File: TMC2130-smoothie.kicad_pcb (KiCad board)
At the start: 4 copper layers, 55 parts, among them P1 CONN_01X04, U1 TMC2130

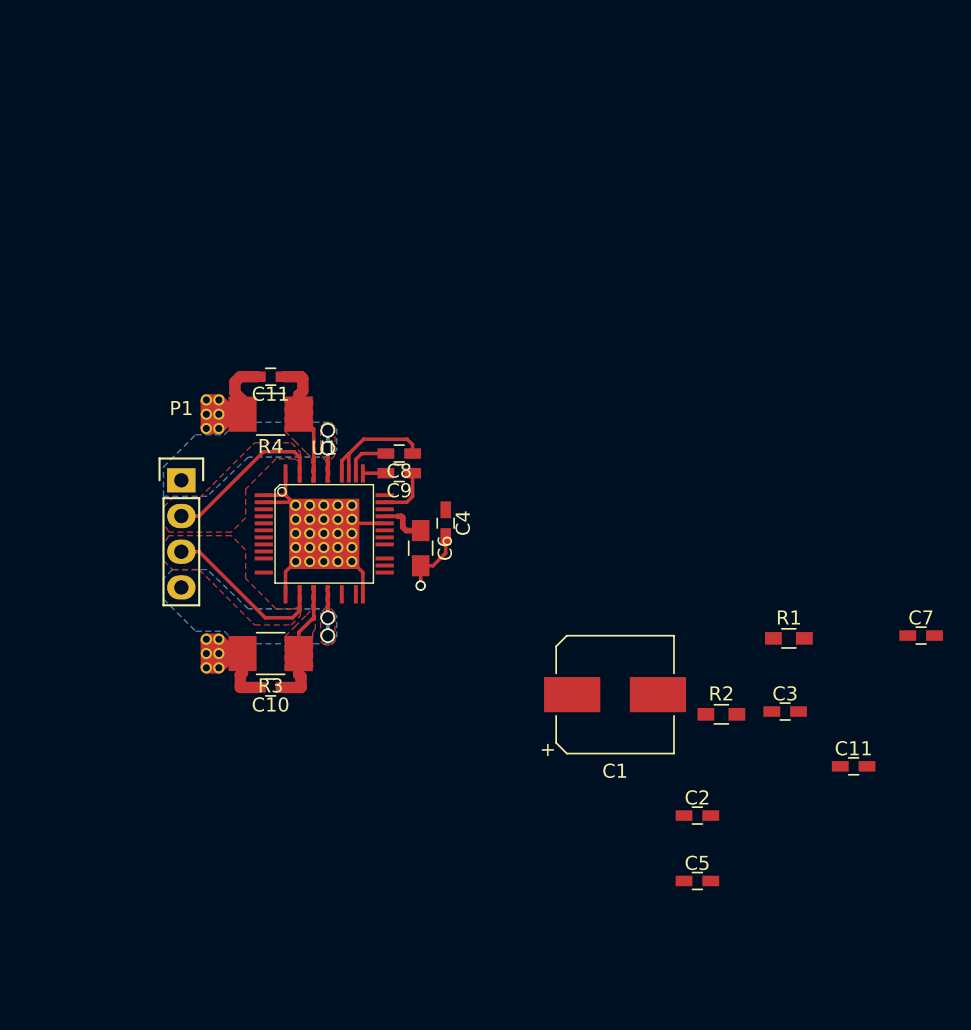
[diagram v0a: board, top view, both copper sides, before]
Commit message: Initial layout of 1-driver
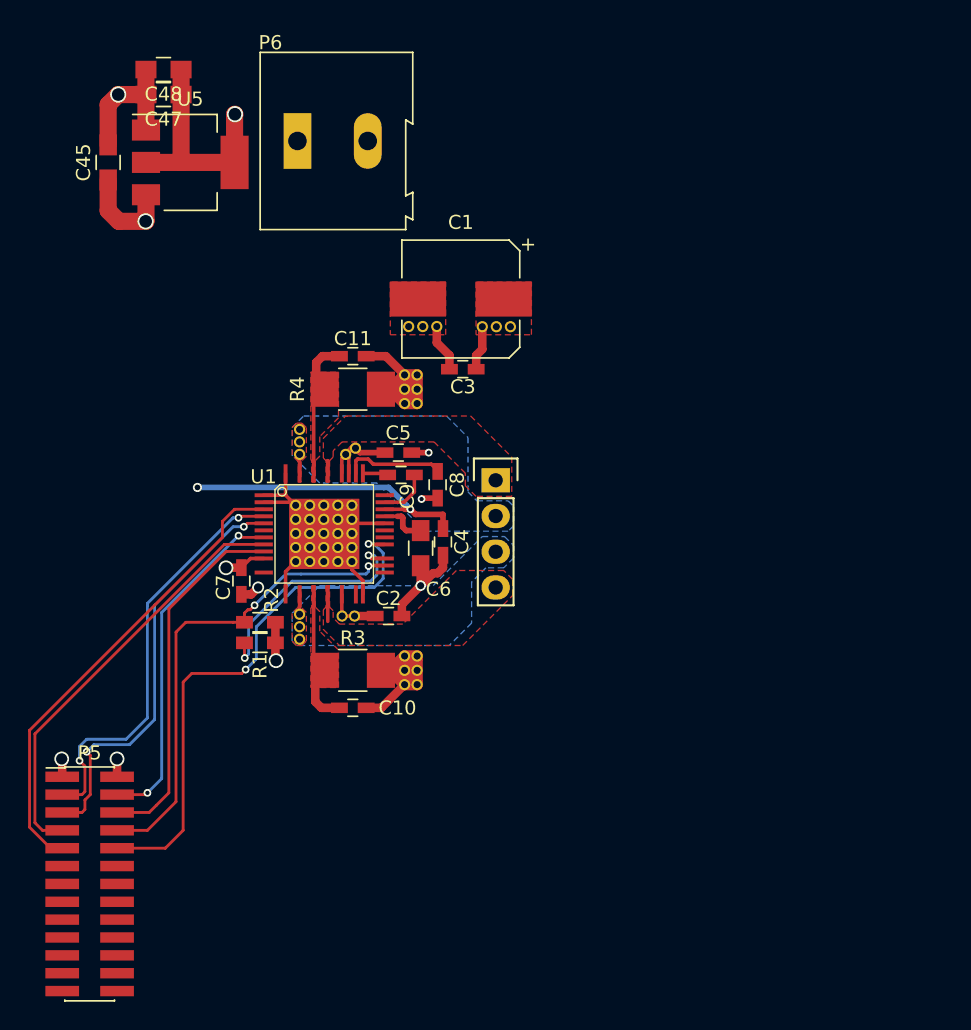
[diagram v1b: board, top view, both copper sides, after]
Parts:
- removed the C10 at (250.2, 163.3)
- added C45: 10uF, Capacitors_SMD:C_0805_HandSoldering, F.Cu at (238.6, 126.0)
- added C47: 10uF, Capacitors_SMD:C_0805_HandSoldering, F.Cu at (242.6, 121.2)
- added C48: 10uF, Capacitors_SMD:C_0805_HandSoldering, F.Cu at (242.6, 119.4)
- added P5: CONN_01X26, Pin_Headers:Pin_Header_Straight_2x13_Pitch1.27mm_SMD, F.Cu at (237.3, 177.3)
- added P6: Vmot, Connect:AK300-2, F.Cu at (252.1, 124.5)
- added REF**: VIA 0.5d0.8p, VIA 0.5d0.8p, F.Cu at (256.2, 146.3)
- added REF**: VIA 0.5d0.8p, VIA 0.5d0.8p, F.Cu at (252.2, 145.9)
- added REF**: VIA 0.5d0.8p, VIA 0.5d0.8p, F.Cu at (252.2, 145.0)
- added REF**: VIA 0.5d0.8p, VIA 0.5d0.8p, F.Cu at (252.2, 146.7)
- added REF**: VIA 0.5d0.8p, VIA 0.5d0.8p, F.Cu at (255.5, 146.7)
- added REF**: VIA 0.5d0.8p, VIA 0.5d0.8p, F.Cu at (256.2, 158.2)
- added REF**: VIA 0.5d0.8p, VIA 0.5d0.8p, F.Cu at (255.3, 158.2)
- added REF**: VIA 0.5d0.8p, VIA 0.5d0.8p, F.Cu at (252.2, 159.0)
- added REF**: VIA 0.5d0.8p, VIA 0.5d0.8p, F.Cu at (252.2, 158.1)
- added REF**: VIA 0.5d0.8p, VIA 0.5d0.8p, F.Cu at (252.2, 159.9)
- added REF**11111: VIA 0.5d0.8p, VIA 0.5d0.8p, F.Cu at (265.2, 137.7)
- added REF**11121: VIA 0.5d0.8p, VIA 0.5d0.8p, F.Cu at (266.2, 137.7)
- added REF**11131: VIA 0.5d0.8p, VIA 0.5d0.8p, F.Cu at (267.2, 137.7)
- added REF**121: VIA 0.5d0.8p, VIA 0.5d0.8p, F.Cu at (260.0, 137.7)
- added REF**131: VIA 0.5d0.8p, VIA 0.5d0.8p, F.Cu at (261.0, 137.7)
- added REF**141: VIA 0.5d0.8p, VIA 0.5d0.8p, F.Cu at (262.0, 137.7)
- added U5: AP1117-3v3, TO_SOT_Packages_SMD:SOT-223-3Lead_TabPin2, F.Cu at (244.5, 126.0)
- moved C7 48.5 mm to (248.1, 155.8), turned to 270 degrees
- moved C11 46.0 mm to (256.0, 139.8)
- moved R2 37.6 mm to (249.4, 158.7)
- moved C5 37.1 mm to (259.3, 146.6)
- moved C3 33.4 mm to (263.9, 140.7), turned to 180 degrees
- moved R1 33.2 mm to (249.4, 160.1)
- moved C1 30.2 mm to (263.7, 135.7), turned to 180 degrees
- moved C2 26.1 mm to (258.6, 158.2)
- moved REF** 25.7 mm to (260.6, 141.1), turned to 180 degrees
- moved REF** 25.2 mm to (260.6, 163.1), turned to 180 degrees
- moved REF** 24.7 mm to (259.7, 141.1), turned to 180 degrees
- moved C10 24.3 mm to (256.0, 164.8), turned to 0 degrees
- moved REF** 24.2 mm to (259.7, 163.1), turned to 180 degrees
- moved REF** 24.0 mm to (260.6, 142.1), turned to 180 degrees
- moved REF** 23.6 mm to (260.6, 162.1), turned to 180 degrees
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- renumbered C11 to C10, R2 to R1, R1 to R2, R4 to R3, R3 to R4
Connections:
- C10 pad 1: Net-(C11-Pad1) -> Net-(C10-Pad1)
- C7 pad 1: Net-(C7-Pad1) -> +3V3
- R1 pad 1: M1_DIAG0 -> M1_DIAG1
- R2 pad 1: M1_DIAG1 -> M1_DIAG0
- R3 pad 1: Net-(C11-Pad1) -> Net-(C10-Pad1)
- R4 pad 1: Net-(C10-Pad1) -> Net-(C11-Pad1)
- U1 pad 10: Net-(C7-Pad1) -> +3V3
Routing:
- net M1_EN: track 0.00 -> 38.7 mm, vias 0 -> 2
- net M1_DIAG0: track 0.00 -> 34.5 mm, vias 0 -> 2
- net SPI_CS_M1: track 0.00 -> 33.7 mm
- net M1_STEP: track 0.00 -> 30.3 mm
- net SPI_MOSI: track 0.00 -> 30.2 mm, vias 0 -> 2
- net SPI_SCK: track 0.00 -> 29.7 mm, vias 0 -> 2
- net +5V: track 0.00 -> 29.4 mm, vias 0 -> 4
- net M1_DIR: track 0.00 -> 25.8 mm
- net SPI_MISO: track 0.00 -> 25.0 mm, vias 0 -> 2
- net +3V3: track 0.00 -> 22.1 mm, vias 0 -> 3
- net M1_DIAG1: track 0.00 -> 17.3 mm, vias 0 -> 2
- net GND: track 66.1 -> 82.0 mm, vias 1 -> 5
- net /Driver1/OB1: track 11.7 -> 1.42 mm
- net /Driver1/OA1: track 11.6 -> 1.35 mm
- net +24V: track 8.76 -> 14.3 mm, vias 0 -> 1
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- added copper zone on F.Cu, net +24V
- added copper zone on In2.Cu, net +24V
- added copper zone on In2.Cu, net +3V3
- added copper zone on In2.Cu, net +5V
- added copper zone on B.Cu, net /Driver1/OA1
- added copper zone on B.Cu, net /Driver1/OB1
- added copper zone on F.Cu, net GND
- removed copper zone on B.Cu, net /Driver1/OA2
- removed copper zone on B.Cu, net /Driver1/OB2

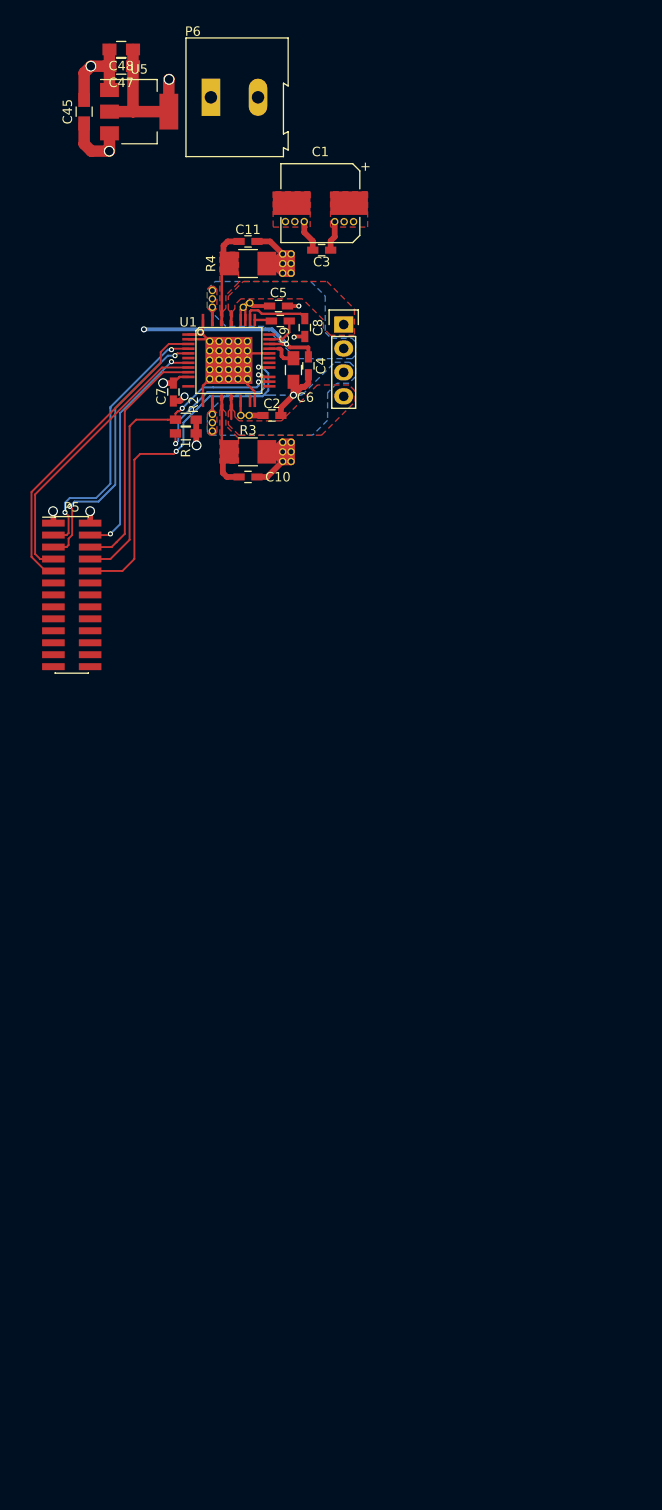
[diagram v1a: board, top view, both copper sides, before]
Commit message: Routed entire PCB
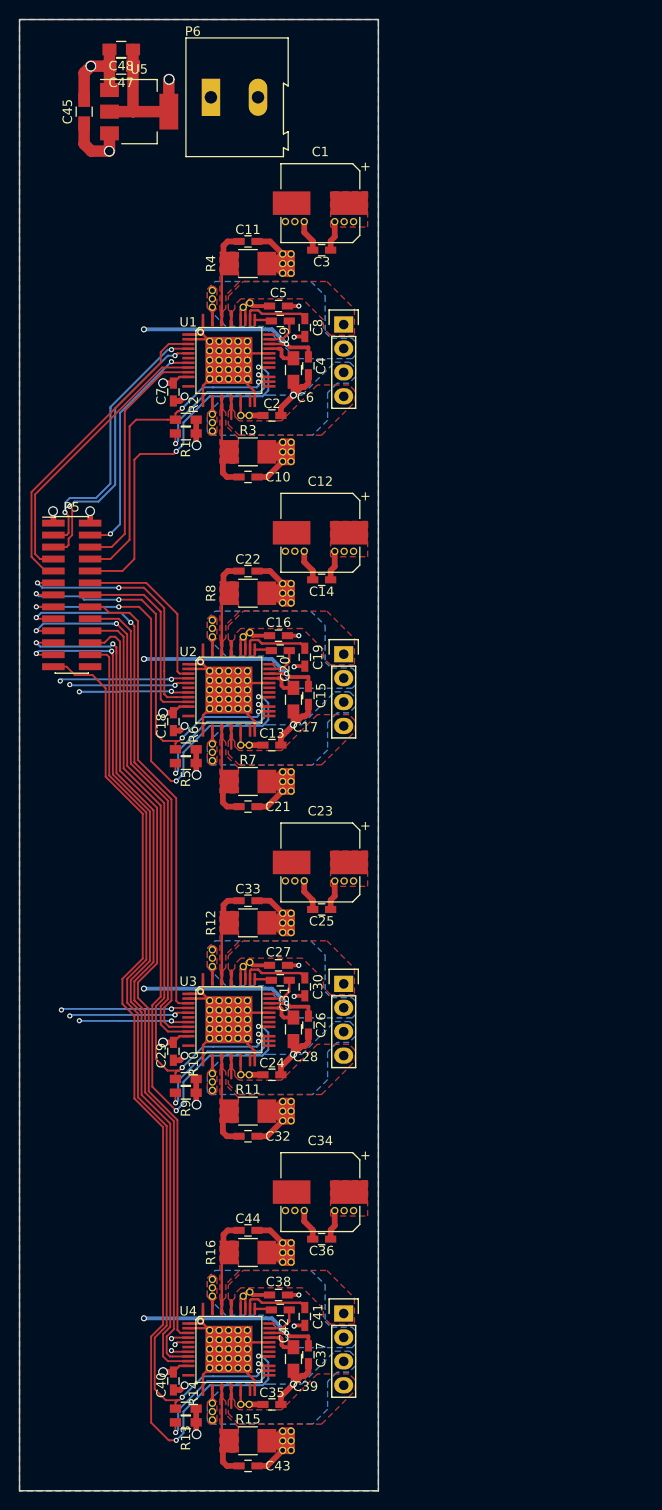
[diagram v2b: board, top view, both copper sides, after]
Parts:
- added C12: 100uF, Capacitors_SMD:CP_Elec_8x10, F.Cu at (263.7, 170.7)
- added C13: 100nF, Capacitors_SMD:C_0603_HandSoldering, F.Cu at (258.6, 193.2)
- added C14: 100nF, Capacitors_SMD:C_0603_HandSoldering, F.Cu at (263.9, 175.7)
- added C15: 470nF, Capacitors_SMD:C_0603_HandSoldering, F.Cu at (262.4, 188.0)
- added C16: 100nF, Capacitors_SMD:C_0603_HandSoldering, F.Cu at (259.3, 181.6)
- added C17: 4.7uF, Capacitors_SMD:C_0805_HandSoldering, F.Cu at (260.9, 188.4)
- added C18: 100nF, Capacitors_SMD:C_0603_HandSoldering, F.Cu at (248.1, 190.8)
- added C19: 100nF, Capacitors_SMD:C_0603_HandSoldering, F.Cu at (262.1, 183.9)
- added C20: 22nF, Capacitors_SMD:C_0603_HandSoldering, F.Cu at (259.5, 183.2)
- added C21: 100nF, Capacitors_SMD:C_0603_HandSoldering, F.Cu at (256.0, 199.8)
- added C22: 100nF, Capacitors_SMD:C_0603_HandSoldering, F.Cu at (256.0, 174.8)
- added C23: 100uF, Capacitors_SMD:CP_Elec_8x10, F.Cu at (263.7, 205.7)
- added C24: 100nF, Capacitors_SMD:C_0603_HandSoldering, F.Cu at (258.6, 228.2)
- added C25: 100nF, Capacitors_SMD:C_0603_HandSoldering, F.Cu at (263.9, 210.7)
- added C26: 470nF, Capacitors_SMD:C_0603_HandSoldering, F.Cu at (262.4, 223.0)
- added C27: 100nF, Capacitors_SMD:C_0603_HandSoldering, F.Cu at (259.3, 216.6)
- added C28: 4.7uF, Capacitors_SMD:C_0805_HandSoldering, F.Cu at (260.9, 223.4)
- added C29: 100nF, Capacitors_SMD:C_0603_HandSoldering, F.Cu at (248.1, 225.8)
- added C30: 100nF, Capacitors_SMD:C_0603_HandSoldering, F.Cu at (262.1, 218.9)
- added C31: 22nF, Capacitors_SMD:C_0603_HandSoldering, F.Cu at (259.5, 218.2)
- added C32: 100nF, Capacitors_SMD:C_0603_HandSoldering, F.Cu at (256.0, 234.8)
- added C33: 100nF, Capacitors_SMD:C_0603_HandSoldering, F.Cu at (256.0, 209.8)
- added C34: 100uF, Capacitors_SMD:CP_Elec_8x10, F.Cu at (263.7, 240.7)
- added C35: 100nF, Capacitors_SMD:C_0603_HandSoldering, F.Cu at (258.6, 263.2)
- added C36: 100nF, Capacitors_SMD:C_0603_HandSoldering, F.Cu at (263.9, 245.7)
- added C37: 470nF, Capacitors_SMD:C_0603_HandSoldering, F.Cu at (262.4, 258.0)
- added C38: 100nF, Capacitors_SMD:C_0603_HandSoldering, F.Cu at (259.3, 251.6)
- added C39: 4.7uF, Capacitors_SMD:C_0805_HandSoldering, F.Cu at (260.9, 258.4)
- added C40: 100nF, Capacitors_SMD:C_0603_HandSoldering, F.Cu at (248.1, 260.8)
- added C41: 100nF, Capacitors_SMD:C_0603_HandSoldering, F.Cu at (262.1, 253.9)
- added C42: 22nF, Capacitors_SMD:C_0603_HandSoldering, F.Cu at (259.5, 253.2)
- added C43: 100nF, Capacitors_SMD:C_0603_HandSoldering, F.Cu at (256.0, 269.8)
- added C44: 100nF, Capacitors_SMD:C_0603_HandSoldering, F.Cu at (256.0, 244.8)
- added P2: CONN_01X04, Pin_Headers:Pin_Header_Straight_1x04, F.Cu at (266.2, 183.6)
- added P3: CONN_01X04, Pin_Headers:Pin_Header_Straight_1x04, F.Cu at (266.2, 218.6)
- added P4: CONN_01X04, Pin_Headers:Pin_Header_Straight_1x04, F.Cu at (266.2, 253.6)
- added R10: 47k, Resistors_SMD:R_0603_HandSoldering, F.Cu at (249.4, 228.7)
- added R11: 0.33R 0.5W, Resistors_SMD:R_1210_HandSoldering, F.Cu at (256.0, 232.1)
- added R12: 0.33R 0.5W, Resistors_SMD:R_1210_HandSoldering, F.Cu at (256.0, 212.1)
- added R13: 47k, Resistors_SMD:R_0603_HandSoldering, F.Cu at (249.4, 265.1)
- added R14: 47k, Resistors_SMD:R_0603_HandSoldering, F.Cu at (249.4, 263.7)
- added R15: 0.33R 0.5W, Resistors_SMD:R_1210_HandSoldering, F.Cu at (256.0, 267.1)
- added R16: 0.33R 0.5W, Resistors_SMD:R_1210_HandSoldering, F.Cu at (256.0, 247.1)
- added R5: 47k, Resistors_SMD:R_0603_HandSoldering, F.Cu at (249.4, 195.1)
- added R6: 47k, Resistors_SMD:R_0603_HandSoldering, F.Cu at (249.4, 193.7)
- added R7: 0.33R 0.5W, Resistors_SMD:R_1210_HandSoldering, F.Cu at (256.0, 197.1)
- added R8: 0.33R 0.5W, Resistors_SMD:R_1210_HandSoldering, F.Cu at (256.0, 177.1)
- added R9: 47k, Resistors_SMD:R_0603_HandSoldering, F.Cu at (249.4, 230.1)
- added REF**11112: VIA 0.5d0.8p, VIA 0.5d0.8p, F.Cu at (265.2, 172.7)
- added REF**11113: VIA 0.5d0.8p, VIA 0.5d0.8p, F.Cu at (265.2, 207.7)
- added REF**11114: VIA 0.5d0.8p, VIA 0.5d0.8p, F.Cu at (265.2, 242.7)
- added REF**11122: VIA 0.5d0.8p, VIA 0.5d0.8p, F.Cu at (266.2, 172.7)
- added REF**11123: VIA 0.5d0.8p, VIA 0.5d0.8p, F.Cu at (266.2, 207.7)
- added REF**11124: VIA 0.5d0.8p, VIA 0.5d0.8p, F.Cu at (266.2, 242.7)
- added REF**11132: VIA 0.5d0.8p, VIA 0.5d0.8p, F.Cu at (267.2, 172.7)
- added REF**11133: VIA 0.5d0.8p, VIA 0.5d0.8p, F.Cu at (267.2, 207.7)
- added REF**11134: VIA 0.5d0.8p, VIA 0.5d0.8p, F.Cu at (267.2, 242.7)
- added REF**1210: VIA 0.5d0.8p, VIA 0.5d0.8p, F.Cu at (260.0, 172.7)
- added REF**1211: VIA 0.5d0.8p, VIA 0.5d0.8p, F.Cu at (260.0, 207.7)
- added REF**1212: VIA 0.5d0.8p, VIA 0.5d0.8p, F.Cu at (260.0, 242.7)
- added REF**122: VIA 0.5d0.8p, VIA 0.5d0.8p, F.Cu at (255.3, 193.2)
- added REF**123: VIA 0.5d0.8p, VIA 0.5d0.8p, F.Cu at (255.3, 228.2)
- added REF**124: VIA 0.5d0.8p, VIA 0.5d0.8p, F.Cu at (255.3, 263.2)
- added REF**125: VIA 0.5d0.8p, VIA 0.5d0.8p, F.Cu at (256.2, 193.2)
- added REF**126: VIA 0.5d0.8p, VIA 0.5d0.8p, F.Cu at (256.2, 228.2)
- added REF**127: VIA 0.5d0.8p, VIA 0.5d0.8p, F.Cu at (256.2, 263.2)
- added REF**128: VIA 0.5d0.8p, VIA 0.5d0.8p, F.Cu at (256.0, 185.4)
- added REF**129: VIA 0.5d0.8p, VIA 0.5d0.8p, F.Cu at (256.0, 220.4)
- added REF**130: VIA 0.5d0.8p, VIA 0.5d0.8p, F.Cu at (256.0, 255.4)
- added REF**1310: VIA 0.5d0.8p, VIA 0.5d0.8p, F.Cu at (261.0, 172.7)
- added REF**1311: VIA 0.5d0.8p, VIA 0.5d0.8p, F.Cu at (261.0, 207.7)
- added REF**1312: VIA 0.5d0.8p, VIA 0.5d0.8p, F.Cu at (261.0, 242.7)
- added REF**132: VIA 0.5d0.8p, VIA 0.5d0.8p, F.Cu at (256.0, 187.4)
- added REF**133: VIA 0.5d0.8p, VIA 0.5d0.8p, F.Cu at (256.0, 222.4)
- added REF**134: VIA 0.5d0.8p, VIA 0.5d0.8p, F.Cu at (256.0, 257.4)
- added REF**135: VIA 0.5d0.8p, VIA 0.5d0.8p, F.Cu at (256.0, 186.4)
- added REF**136: VIA 0.5d0.8p, VIA 0.5d0.8p, F.Cu at (256.0, 221.4)
- added REF**137: VIA 0.5d0.8p, VIA 0.5d0.8p, F.Cu at (256.0, 256.4)
- added REF**138: VIA 0.5d0.8p, VIA 0.5d0.8p, F.Cu at (252.0, 187.4)
- added REF**139: VIA 0.5d0.8p, VIA 0.5d0.8p, F.Cu at (252.0, 222.4)
- added REF**140: VIA 0.5d0.8p, VIA 0.5d0.8p, F.Cu at (252.0, 257.4)
- added REF**1410: VIA 0.5d0.8p, VIA 0.5d0.8p, F.Cu at (262.0, 172.7)
- added REF**1411: VIA 0.5d0.8p, VIA 0.5d0.8p, F.Cu at (262.0, 207.7)
- added REF**1412: VIA 0.5d0.8p, VIA 0.5d0.8p, F.Cu at (262.0, 242.7)
- added REF**142: VIA 0.5d0.8p, VIA 0.5d0.8p, F.Cu at (253.0, 187.4)
- added REF**143: VIA 0.5d0.8p, VIA 0.5d0.8p, F.Cu at (253.0, 222.4)
- added REF**144: VIA 0.5d0.8p, VIA 0.5d0.8p, F.Cu at (253.0, 257.4)
- added REF**145: VIA 0.5d0.8p, VIA 0.5d0.8p, F.Cu at (253.0, 186.4)
- added REF**146: VIA 0.5d0.8p, VIA 0.5d0.8p, F.Cu at (253.0, 221.4)
- added REF**147: VIA 0.5d0.8p, VIA 0.5d0.8p, F.Cu at (253.0, 256.4)
- added REF**148: VIA 0.5d0.8p, VIA 0.5d0.8p, F.Cu at (252.0, 186.4)
- added REF**149: VIA 0.5d0.8p, VIA 0.5d0.8p, F.Cu at (252.0, 221.4)
- added REF**150: VIA 0.5d0.8p, VIA 0.5d0.8p, F.Cu at (252.0, 256.4)
- added REF**151: VIA 0.5d0.8p, VIA 0.5d0.8p, F.Cu at (253.0, 185.4)
- added REF**152: VIA 0.5d0.8p, VIA 0.5d0.8p, F.Cu at (253.0, 220.4)
- added REF**153: VIA 0.5d0.8p, VIA 0.5d0.8p, F.Cu at (253.0, 255.4)
- added REF**154: VIA 0.5d0.8p, VIA 0.5d0.8p, F.Cu at (252.0, 185.4)
- added REF**155: VIA 0.5d0.8p, VIA 0.5d0.8p, F.Cu at (252.0, 220.4)
- added REF**156: VIA 0.5d0.8p, VIA 0.5d0.8p, F.Cu at (252.0, 255.4)
- added REF**157: VIA 0.5d0.8p, VIA 0.5d0.8p, F.Cu at (254.0, 189.4)
- added REF**158: VIA 0.5d0.8p, VIA 0.5d0.8p, F.Cu at (254.0, 224.4)
- added REF**159: VIA 0.5d0.8p, VIA 0.5d0.8p, F.Cu at (254.0, 259.4)
- added REF**160: VIA 0.5d0.8p, VIA 0.5d0.8p, F.Cu at (254.0, 188.4)
- added REF**161: VIA 0.5d0.8p, VIA 0.5d0.8p, F.Cu at (254.0, 223.4)
- added REF**162: VIA 0.5d0.8p, VIA 0.5d0.8p, F.Cu at (254.0, 258.4)
- added REF**163: VIA 0.5d0.8p, VIA 0.5d0.8p, F.Cu at (255.0, 188.4)
- added REF**164: VIA 0.5d0.8p, VIA 0.5d0.8p, F.Cu at (255.0, 223.4)
- added REF**165: VIA 0.5d0.8p, VIA 0.5d0.8p, F.Cu at (255.0, 258.4)
- added REF**166: VIA 0.5d0.8p, VIA 0.5d0.8p, F.Cu at (256.0, 189.4)
- added REF**167: VIA 0.5d0.8p, VIA 0.5d0.8p, F.Cu at (256.0, 224.4)
- added REF**168: VIA 0.5d0.8p, VIA 0.5d0.8p, F.Cu at (256.0, 259.4)
- added REF**169: VIA 0.5d0.8p, VIA 0.5d0.8p, F.Cu at (255.0, 189.4)
- added REF**170: VIA 0.5d0.8p, VIA 0.5d0.8p, F.Cu at (255.0, 224.4)
- added REF**171: VIA 0.5d0.8p, VIA 0.5d0.8p, F.Cu at (255.0, 259.4)
- added REF**172: VIA 0.5d0.8p, VIA 0.5d0.8p, F.Cu at (256.0, 188.4)
- added REF**173: VIA 0.5d0.8p, VIA 0.5d0.8p, F.Cu at (256.0, 223.4)
- added REF**174: VIA 0.5d0.8p, VIA 0.5d0.8p, F.Cu at (256.0, 258.4)
- added REF**175: VIA 0.5d0.8p, VIA 0.5d0.8p, F.Cu at (255.0, 187.4)
- added REF**176: VIA 0.5d0.8p, VIA 0.5d0.8p, F.Cu at (255.0, 222.4)
- added REF**177: VIA 0.5d0.8p, VIA 0.5d0.8p, F.Cu at (255.0, 257.4)
- added REF**178: VIA 0.5d0.8p, VIA 0.5d0.8p, F.Cu at (254.0, 186.4)
- added REF**179: VIA 0.5d0.8p, VIA 0.5d0.8p, F.Cu at (254.0, 221.4)
- added REF**180: VIA 0.5d0.8p, VIA 0.5d0.8p, F.Cu at (254.0, 256.4)
- added REF**181: VIA 0.5d0.8p, VIA 0.5d0.8p, F.Cu at (255.0, 185.4)
- added REF**182: VIA 0.5d0.8p, VIA 0.5d0.8p, F.Cu at (255.0, 220.4)
- added REF**183: VIA 0.5d0.8p, VIA 0.5d0.8p, F.Cu at (255.0, 255.4)
- added REF**184: VIA 0.5d0.8p, VIA 0.5d0.8p, F.Cu at (255.0, 186.4)
- added REF**185: VIA 0.5d0.8p, VIA 0.5d0.8p, F.Cu at (255.0, 221.4)
- added REF**186: VIA 0.5d0.8p, VIA 0.5d0.8p, F.Cu at (255.0, 256.4)
- added REF**187: VIA 0.5d0.8p, VIA 0.5d0.8p, F.Cu at (254.0, 187.4)
- added REF**188: VIA 0.5d0.8p, VIA 0.5d0.8p, F.Cu at (254.0, 222.4)
- added REF**189: VIA 0.5d0.8p, VIA 0.5d0.8p, F.Cu at (254.0, 257.4)
- added REF**190: VIA 0.5d0.8p, VIA 0.5d0.8p, F.Cu at (254.0, 185.4)
- added REF**191: VIA 0.5d0.8p, VIA 0.5d0.8p, F.Cu at (254.0, 220.4)
- added REF**192: VIA 0.5d0.8p, VIA 0.5d0.8p, F.Cu at (254.0, 255.4)
- added REF**193: VIA 0.5d0.8p, VIA 0.5d0.8p, F.Cu at (252.2, 193.1)
- added REF**194: VIA 0.5d0.8p, VIA 0.5d0.8p, F.Cu at (252.2, 228.1)
- added REF**195: VIA 0.5d0.8p, VIA 0.5d0.8p, F.Cu at (252.2, 263.1)
- added REF**196: VIA 0.5d0.8p, VIA 0.5d0.8p, F.Cu at (252.2, 194.9)
- added REF**197: VIA 0.5d0.8p, VIA 0.5d0.8p, F.Cu at (252.2, 229.9)
- added REF**198: VIA 0.5d0.8p, VIA 0.5d0.8p, F.Cu at (252.2, 264.9)
- added REF**199: VIA 0.5d0.8p, VIA 0.5d0.8p, F.Cu at (252.2, 194.0)
- added REF**200: VIA 0.5d0.8p, VIA 0.5d0.8p, F.Cu at (252.2, 229.0)
- added REF**201: VIA 0.5d0.8p, VIA 0.5d0.8p, F.Cu at (252.2, 264.0)
- added REF**202: VIA 0.5d0.8p, VIA 0.5d0.8p, F.Cu at (260.6, 198.1)
- added REF**203: VIA 0.5d0.8p, VIA 0.5d0.8p, F.Cu at (260.6, 233.1)
- added REF**204: VIA 0.5d0.8p, VIA 0.5d0.8p, F.Cu at (260.6, 268.1)
- added REF**205: VIA 0.5d0.8p, VIA 0.5d0.8p, F.Cu at (259.7, 198.1)
- added REF**206: VIA 0.5d0.8p, VIA 0.5d0.8p, F.Cu at (259.7, 233.1)
- added REF**207: VIA 0.5d0.8p, VIA 0.5d0.8p, F.Cu at (259.7, 268.1)
- added REF**208: VIA 0.5d0.8p, VIA 0.5d0.8p, F.Cu at (260.6, 196.1)
- added REF**209: VIA 0.5d0.8p, VIA 0.5d0.8p, F.Cu at (260.6, 231.1)
- added REF**210: VIA 0.5d0.8p, VIA 0.5d0.8p, F.Cu at (260.6, 266.1)
- added REF**211: VIA 0.5d0.8p, VIA 0.5d0.8p, F.Cu at (259.7, 196.1)
- added REF**212: VIA 0.5d0.8p, VIA 0.5d0.8p, F.Cu at (259.7, 231.1)
- added REF**213: VIA 0.5d0.8p, VIA 0.5d0.8p, F.Cu at (259.7, 266.1)
- added REF**214: VIA 0.5d0.8p, VIA 0.5d0.8p, F.Cu at (260.6, 197.1)
- added REF**215: VIA 0.5d0.8p, VIA 0.5d0.8p, F.Cu at (260.6, 232.1)
- added REF**216: VIA 0.5d0.8p, VIA 0.5d0.8p, F.Cu at (260.6, 267.1)
- added REF**217: VIA 0.5d0.8p, VIA 0.5d0.8p, F.Cu at (259.7, 197.1)
- added REF**218: VIA 0.5d0.8p, VIA 0.5d0.8p, F.Cu at (259.7, 232.1)
- added REF**219: VIA 0.5d0.8p, VIA 0.5d0.8p, F.Cu at (259.7, 267.1)
- added REF**220: VIA 0.5d0.8p, VIA 0.5d0.8p, F.Cu at (253.0, 189.4)
- added REF**221: VIA 0.5d0.8p, VIA 0.5d0.8p, F.Cu at (253.0, 224.4)
- added REF**222: VIA 0.5d0.8p, VIA 0.5d0.8p, F.Cu at (253.0, 259.4)
- added REF**223: VIA 0.5d0.8p, VIA 0.5d0.8p, F.Cu at (252.0, 189.4)
- added REF**224: VIA 0.5d0.8p, VIA 0.5d0.8p, F.Cu at (252.0, 224.4)
- added REF**225: VIA 0.5d0.8p, VIA 0.5d0.8p, F.Cu at (252.0, 259.4)
- added REF**226: VIA 0.5d0.8p, VIA 0.5d0.8p, F.Cu at (252.0, 188.4)
- added REF**227: VIA 0.5d0.8p, VIA 0.5d0.8p, F.Cu at (252.0, 223.4)
- added REF**228: VIA 0.5d0.8p, VIA 0.5d0.8p, F.Cu at (252.0, 258.4)
- added REF**229: VIA 0.5d0.8p, VIA 0.5d0.8p, F.Cu at (253.0, 188.4)
- added REF**230: VIA 0.5d0.8p, VIA 0.5d0.8p, F.Cu at (253.0, 223.4)
- added REF**231: VIA 0.5d0.8p, VIA 0.5d0.8p, F.Cu at (253.0, 258.4)
- added REF**232: VIA 0.5d0.8p, VIA 0.5d0.8p, F.Cu at (252.2, 181.7)
- added REF**232: VIA 0.5d0.8p, VIA 0.5d0.8p, F.Cu at (252.2, 180.8)
- added REF**232: VIA 0.5d0.8p, VIA 0.5d0.8p, F.Cu at (252.2, 180.0)
- added REF**233: VIA 0.5d0.8p, VIA 0.5d0.8p, F.Cu at (252.2, 216.7)
- added REF**234: VIA 0.5d0.8p, VIA 0.5d0.8p, F.Cu at (252.2, 251.7)
- added REF**235: VIA 0.5d0.8p, VIA 0.5d0.8p, F.Cu at (256.2, 181.3)
- added REF**236: VIA 0.5d0.8p, VIA 0.5d0.8p, F.Cu at (256.2, 216.3)
- added REF**237: VIA 0.5d0.8p, VIA 0.5d0.8p, F.Cu at (256.2, 251.3)
- added REF**238: VIA 0.5d0.8p, VIA 0.5d0.8p, F.Cu at (255.5, 181.7)
- added REF**239: VIA 0.5d0.8p, VIA 0.5d0.8p, F.Cu at (255.5, 216.7)
- added REF**240: VIA 0.5d0.8p, VIA 0.5d0.8p, F.Cu at (255.5, 251.7)
- added REF**242: VIA 0.5d0.8p, VIA 0.5d0.8p, F.Cu at (252.2, 215.9)
- added REF**243: VIA 0.5d0.8p, VIA 0.5d0.8p, F.Cu at (252.2, 250.9)
- added REF**245: VIA 0.5d0.8p, VIA 0.5d0.8p, F.Cu at (252.2, 215.0)
- added REF**246: VIA 0.5d0.8p, VIA 0.5d0.8p, F.Cu at (252.2, 250.0)
- added REF**247: VIA 0.5d0.8p, VIA 0.5d0.8p, F.Cu at (259.7, 177.1)
- added REF**248: VIA 0.5d0.8p, VIA 0.5d0.8p, F.Cu at (259.7, 212.1)
- added REF**249: VIA 0.5d0.8p, VIA 0.5d0.8p, F.Cu at (259.7, 247.1)
- added REF**250: VIA 0.5d0.8p, VIA 0.5d0.8p, F.Cu at (260.6, 178.1)
- added REF**251: VIA 0.5d0.8p, VIA 0.5d0.8p, F.Cu at (260.6, 213.1)
- added REF**252: VIA 0.5d0.8p, VIA 0.5d0.8p, F.Cu at (260.6, 248.1)
- added REF**253: VIA 0.5d0.8p, VIA 0.5d0.8p, F.Cu at (260.6, 177.1)
- added REF**254: VIA 0.5d0.8p, VIA 0.5d0.8p, F.Cu at (260.6, 212.1)
- added REF**255: VIA 0.5d0.8p, VIA 0.5d0.8p, F.Cu at (260.6, 247.1)
- added REF**256: VIA 0.5d0.8p, VIA 0.5d0.8p, F.Cu at (259.7, 178.1)
- added REF**257: VIA 0.5d0.8p, VIA 0.5d0.8p, F.Cu at (259.7, 213.1)
- added REF**258: VIA 0.5d0.8p, VIA 0.5d0.8p, F.Cu at (259.7, 248.1)
- added REF**259: VIA 0.5d0.8p, VIA 0.5d0.8p, F.Cu at (260.6, 176.1)
- added REF**260: VIA 0.5d0.8p, VIA 0.5d0.8p, F.Cu at (260.6, 211.1)
- added REF**261: VIA 0.5d0.8p, VIA 0.5d0.8p, F.Cu at (260.6, 246.1)
- added REF**262: VIA 0.5d0.8p, VIA 0.5d0.8p, F.Cu at (259.7, 176.1)
- added REF**263: VIA 0.5d0.8p, VIA 0.5d0.8p, F.Cu at (259.7, 211.1)
- added REF**264: VIA 0.5d0.8p, VIA 0.5d0.8p, F.Cu at (259.7, 246.1)
- added U2: TMC2130, trinamic:TMC2130-TQFP, F.Cu at (254.0, 187.4)
- added U3: TMC2130, trinamic:TMC2130-TQFP, F.Cu at (254.0, 222.4)
- added U4: TMC2130, trinamic:TMC2130-TQFP, F.Cu at (254.0, 257.4)
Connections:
- P5 pad 11: M2_DIAG0 -> M2_STEP
- P5 pad 13: M2_DIR -> M2_DIAG0
- P5 pad 14: M2_STEP -> M2_DIR
- P5 pad 16: M3_DIAG0 -> SPI_CS_M3
- P5 pad 17: SPI_CS_M3 -> M3_STEP
- P5 pad 19: M3_STEP -> M3_DIAG0
- P5 pad 21: M4_DIAG0 -> M4_STEP
- P5 pad 24: M4_STEP -> M4_DIAG0
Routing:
- net GND: track 82.0 -> 293.5 mm, vias 5 -> 14
- net SPI_SCK: track 29.7 -> 164.3 mm, vias 2 -> 7
- net SPI_MOSI: track 30.2 -> 159.4 mm, vias 2 -> 7
- net SPI_MISO: track 25.0 -> 151.5 mm, vias 2 -> 7
- net M4_EN: track 0.00 -> 110.9 mm, vias 0 -> 2
- net M4_DIAG0: track 0.00 -> 99.8 mm, vias 0 -> 2
- net M4_STEP: track 0.00 -> 92.7 mm, vias 0 -> 2
- net M4_DIR: track 0.00 -> 92.3 mm, vias 0 -> 2
- net SPI_CS_M4: track 0.00 -> 82.2 mm
- net M3_EN: track 0.00 -> 75.3 mm, vias 0 -> 2
- net M3_DIAG0: track 0.00 -> 74.4 mm, vias 0 -> 4
- net +5V: track 29.4 -> 92.7 mm, vias 4 -> 10
- net M3_STEP: track 0.00 -> 59.8 mm, vias 0 -> 2
- net M3_DIR: track 0.00 -> 51.8 mm
- net M2_EN: track 0.00 -> 51.3 mm, vias 0 -> 4
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- added copper zone on B.Cu, net /Driver2/OA1
- added copper zone on F.Cu, net /Driver2/OA1
- added copper zone on F.Cu, net /Driver2/OA2
- added copper zone on B.Cu, net /Driver2/OB1
- added copper zone on F.Cu, net /Driver2/OB1
- added copper zone on F.Cu, net /Driver2/OB2
- added copper zone on B.Cu, net /Driver3/OA1
- added copper zone on F.Cu, net /Driver3/OA1
- added copper zone on F.Cu, net /Driver3/OA2
- added copper zone on B.Cu, net /Driver3/OB1
- added copper zone on F.Cu, net /Driver3/OB1
- added copper zone on F.Cu, net /Driver3/OB2
- added copper zone on B.Cu, net /Driver4/OA1
- added copper zone on F.Cu, net /Driver4/OA1
- added copper zone on F.Cu, net /Driver4/OA2
- added copper zone on B.Cu, net /Driver4/OB1
- added copper zone on F.Cu, net /Driver4/OB1
- added copper zone on F.Cu, net /Driver4/OB2
- added copper zone on B.Cu, net GND
- added copper zone on F.Cu, net Net-(C21-Pad1)
- added copper zone on F.Cu, net Net-(C22-Pad1)
- added copper zone on F.Cu, net Net-(C32-Pad1)
- added copper zone on F.Cu, net Net-(C33-Pad1)
- added copper zone on F.Cu, net Net-(C43-Pad1)
- added copper zone on F.Cu, net Net-(C44-Pad1)
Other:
- board outline added: 38.1 x 156.2 mm

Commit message: Added gerbers
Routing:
- net M1_DIAG0: track 34.5 -> 36.9 mm
- net M3_DIAG0: track 74.4 -> 76.6 mm
- net M2_DIAG0: track 43.0 -> 45.1 mm
- net M2_EN: track 51.3 -> 53.3 mm
- net M1_EN: track 38.7 -> 40.7 mm
- net M4_DIAG0: track 99.8 -> 101.8 mm
- net M3_EN: track 75.3 -> 77.3 mm
- net SPI_MOSI: track 159.4 -> 161.3 mm
- net M4_EN: track 110.9 -> 112.7 mm
- net M4_DIAG1: track 17.3 -> 19.1 mm
- net M1_DIAG1: track 17.3 -> 19.1 mm
- net M3_DIAG1: track 17.3 -> 19.1 mm
- net M2_DIAG1: track 17.3 -> 19.1 mm
- net SPI_SCK: track 164.3 -> 165.9 mm
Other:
- net class Default: clearance 0.127 -> 0.1524; trace_width 0.127 -> 0.1524; via_dia 0.4572 -> 0.55; via_drill 0.254 -> 0.3
- rule trace_clearance: 0.127 -> 0.1524
- rule trace_min: 0.127 -> 0.1524
- rule via_min_size: 0.4572 -> 0.54991
